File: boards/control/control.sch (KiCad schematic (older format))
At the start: 73 parts, among them U1 SN74ACT08PW, U10 MC74ACT139DG, U11 SN74ACT08PW, U12 SN74ACT08PW, U13 SN74ACT32PW, U14 74ACT00MTCX, U15 MC74ACT139DG, U16 SN74ACT32PW, U2 MC74ACT139DG, U3 MC74ACT86DG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

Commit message: Fix bug in CU schematics
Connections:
- wire segments 122 -> 125
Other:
- moved on the sheet: U16C, U9A
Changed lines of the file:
@@
 L 74xx:74HC00 U9
 U 1 1 5E83EE30
-P 6200 3600
-F 0 "U9" H 6200 3925 50  0000 C CNN
-F 1 "74ACT00MTCX" H 6200 3834 50  0000 C CNN
-F 2 "Package_SO:TSSOP-14_4.4x5mm_P0.65mm" H 6200 3600 50  0001 C CNN
-F 3 "http://www.ti.com/lit/gpn/sn74hc00" H 6200 3600 50  0001 C CNN
-	1    6200 3600
+P 6950 3600
+F 0 "U9" H 6950 3925 50  0000 C CNN
+F 1 "74ACT00MTCX" H 6950 3834 50  0000 C CNN
+F 2 "Package_SO:TSSOP-14_4.4x5mm_P0.65mm" H 6950 3600 50  0001 C CNN
+F 3 "http://www.ti.com/lit/gpn/sn74hc00" H 6950 3600 50  0001 C CNN
+	1    6950 3600
 	1    0    0    -1
 $EndComp
@@
 Text Label 5900 3700 2    50   ~ 0
 ~cycle
-Text Label 6500 3600 0    50   ~ 0
+Text Label 7250 3600 0    50   ~ 0
 ~oe_mem
 Text Label 5900 4050 2    50   ~ 0
@@
 L 74xx:74LS32 U16
 U 3 1 5EAB37A5
-P 8150 12500
-F 0 "U16" H 8150 12825 50  0000 C CNN
-F 1 "SN74ACT32PW" H 8150 12734 50  0000 C CNN
-F 2 "Package_SO:TSSOP-14_4.4x5mm_P0.65mm" H 8150 12500 50  0001 C CNN
-F 3 "http://www.ti.com/lit/gpn/sn74LS32" H 8150 12500 50  0001 C CNN
-	3    8150 12500
+P 6200 3600
+F 0 "U16" H 6200 3925 50  0000 C CNN
+F 1 "SN74ACT32PW" H 6200 3834 50  0000 C CNN
+F 2 "Package_SO:TSSOP-14_4.4x5mm_P0.65mm" H 6200 3600 50  0001 C CNN
+F 3 "http://www.ti.com/lit/gpn/sn74LS32" H 6200 3600 50  0001 C CNN
+	3    6200 3600
 	1    0    0    -1
 $EndComp
@@
 Wire Wire Line
 	2800 4150 2750 4150
+Wire Wire Line
+	6500 3600 6650 3600
+Wire Wire Line
+	6650 3600 6650 3500
+Wire Wire Line
+	6650 3700 6650 3600
 Wire Bus Line
 	3750 2050 3750 2650
 Wire Bus Line
 	3750 1150 3750 1950
+Connection ~ 6650 3600
 $EndSCHEMATC

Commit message: Change control unit schematics to support wait cycles (not checked)
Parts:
- added C11, C12: 0.1u, Capacitor_SMD:C_0805_2012Metric, symbol Device:C
- added D23: KP-2012EC, LED_SMD:LED_0805_2012Metric, symbol Device:LED
- added R23: 620, Resistor_SMD:R_0805_2012Metric, symbol Device:R
- added U17: SN74ACT74D, Package_SO:SOIC-14_3.9x8.7mm_P1.27mm, symbol 74xx:74HC74
- added U18: 74HC02, symbol 74xx:74HC02
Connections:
- net labels added: cycle_d, mem_rdy, we_cycle_d, ~cycle_flip_ena, ~mem_rdy
- wire segments 125 -> 136
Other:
- moved on the sheet: U14C, U3B, U3D

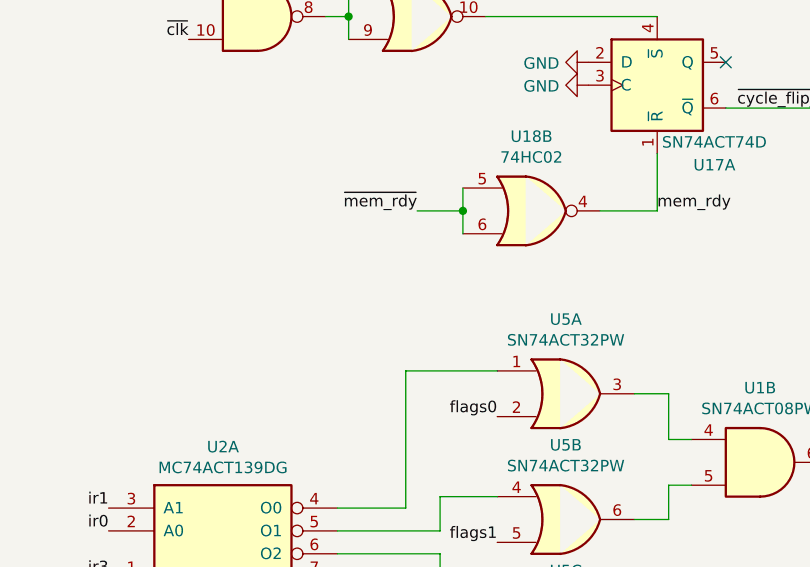
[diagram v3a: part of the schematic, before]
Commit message: Make n_rdy an open-drain pull-up
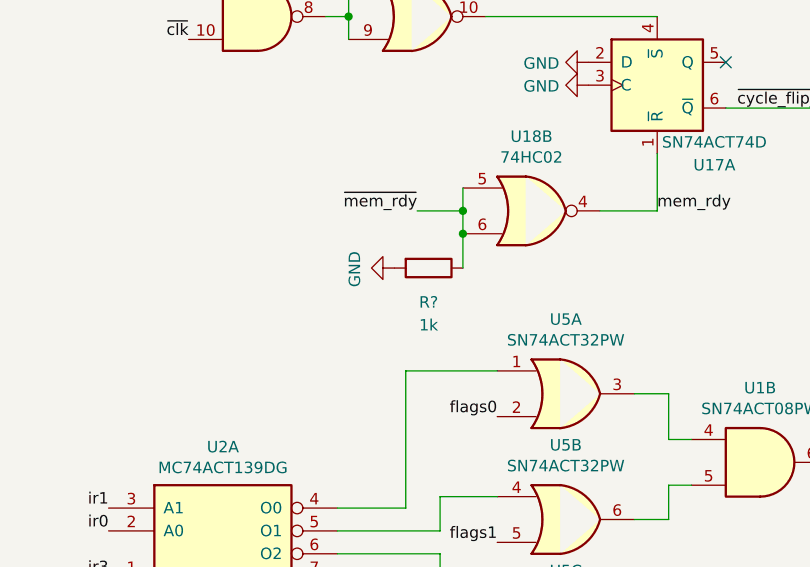
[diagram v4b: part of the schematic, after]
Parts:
- added R?: 1k, Resistor_SMD:R_0805_2012Metric, symbol Device:R
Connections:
- wire segments 136 -> 137
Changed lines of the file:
@@
 	1    0    0    -1
 $EndComp
+Text Label 5050 5850 3    50   ~ 0
+we_cycle_d
+Text Label 1300 8700 1    50   ~ 0
+cycle_d
+$Comp
+L Device:R R?
+U 1 1 60425BE5
+P 2400 10850
+F 0 "R?" V 2550 10850 50  0000 C CNN
+F 1 "1k" V 2650 10850 50  0000 C CNN
+F 2 "Resistor_SMD:R_0805_2012Metric" V 2330 10850 50  0001 C CNN
+F 3 "~" H 2400 10850 50  0001 C CNN
+	1    2400 10850
+	0    1    1    0
+$EndComp
+Wire Wire Line
+	2550 10850 2550 10700
 Wire Bus Line
 	3750 2050 3750 2650
 Wire Bus Line
 	3750 1150 3750 1950
-Text Label 5050 5850 3    50   ~ 0
-we_cycle_d
-Text Label 1300 8700 1    50   ~ 0
-cycle_d
+Connection ~ 2550 10700
+$Comp
+L power:GND #PWR?
+U 1 1 6042F712
+P 2250 10850
+F 0 "#PWR?" H 2250 10600 50  0001 C CNN
+F 1 "GND" H 2255 10677 50  0000 C CNN
+F 2 "" H 2250 10850 50  0001 C CNN
+F 3 "" H 2250 10850 50  0001 C CNN
+	1    2250 10850
+	0    1    1    0
+$EndComp
 $EndSCHEMATC

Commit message: Control: change 74ACT with 74LV-A
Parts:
- U1, U11, U12: value SN74ACT08PW -> 74LV08APWJ
- U10, U15, U2: value MC74ACT139DG -> SN74LV139APWR; footprint Package_SO:SOIC-16_3.9x9.9mm_P1.27mm -> Package_SO:TSSOP-16_4.4x5mm_P0.65mm
- U13, U16, U5, U8: value SN74ACT32PW -> 74LV32APWJ
- U14, U9: value 74ACT00MTCX -> SN74LV00APW
- U17, U4, U6: value SN74ACT74D -> SN74LV74APW; footprint Package_SO:SOIC-14_3.9x8.7mm_P1.27mm -> Package_SO:TSSOP-14_4.4x5mm_P0.65mm
- U18: value 74HC02 -> SN74LV02APWR; footprint (none) -> Package_SO:TSSOP-14_4.4x5mm_P0.65mm
- U3: value MC74ACT86DG -> SN74LV86APWR; footprint Package_SO:SOIC-14_3.9x8.7mm_P1.27mm -> Package_SO:TSSOP-14_4.4x5mm_P0.65mm
- U7: value SN74ACT04PW -> SN74LV04APWR

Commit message: Control: add more capacitors and damping resistors
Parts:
- added C13, C14, C15, C16, C17, C18, C19: 0.1u, Capacitor_SMD:C_0805_2012Metric, symbol Device:C
- added R24, R26: 50, Resistor_SMD:R_0805_2012Metric, symbol Device:R
- gave numbers to parts that had none: 1
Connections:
- wire segments 137 -> 138
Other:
- moved on the sheet: C1, C10, C11, C12, C2, C3, C5, C6, C7, C8, C9

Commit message: Control: PCB rev. 3
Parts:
- added D24: KP-2012CGCK, LED_SMD:LED_0805_2012Metric, symbol Device:LED
- added R27: 600, Resistor_SMD:R_0805_2012Metric, symbol Device:R
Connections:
- net labels added: cycle_flip_ena
- wire segments 138 -> 140
- no-connect marks 13 -> 11
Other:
- moved on the sheet: D21, R21
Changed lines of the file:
@@
 encoding utf-8
 Sheet 1 2
-Title "Control unit - ROM-based"
+Title "Control unit"
 Date "2020-11-29"
 Rev "3"
@@
 NoConn ~ 10650 13100
 $Comp
-L power:GND #PWR040
-U 1 1 60027546
-P 10050 13000
-F 0 "#PWR040" H 10050 12750 50  0001 C CNN
-F 1 "GND" V 10055 12872 50  0000 R CNN
-F 2 "" H 10050 13000 50  0001 C CNN
-F 3 "" H 10050 13000 50  0001 C CNN
-	1    10050 13000
-	0    1    1    0
-$EndComp
-$Comp
-L power:GND #PWR041
-U 1 1 60026D0E
-P 10050 13200
-F 0 "#PWR041" H 10050 12950 50  0001 C CNN
-F 1 "GND" V 10055 13072 50  0000 R CNN
-F 2 "" H 10050 13200 50  0001 C CNN
-F 3 "" H 10050 13200 50  0001 C CNN
-	1    10050 13200
-	0    1    1    0
-$EndComp
-$Comp
 L 74xx:74HC86 U3
 U 4 1 6001AAE8
@@
 Text Label 14700 3650 0    50   ~ 0
 ~we_flags
-NoConn ~ 5150 8600
 NoConn ~ 9550 13100
 NoConn ~ 8450 13150
-$Comp
-L power:GND #PWR0103
-U 1 1 5EB12FC5
-P 8950 13000
-F 0 "#PWR0103" H 8950 12750 50  0001 C CNN
-F 1 "GND" V 8955 12872 50  0000 R CNN
-F 2 "" H 8950 13000 50  0001 C CNN
-F 3 "" H 8950 13000 50  0001 C CNN
-	1    8950 13000
-	0    1    1    0
-$EndComp
-$Comp
-L power:GND #PWR0104
-U 1 1 5EB12FCB
-P 8950 13200
-F 0 "#PWR0104" H 8950 12950 50  0001 C CNN
-F 1 "GND" V 8955 13072 50  0000 R CNN
-F 2 "" H 8950 13200 50  0001 C CNN
-F 3 "" H 8950 13200 50  0001 C CNN
-	1    8950 13200
-	0    1    1    0
-$EndComp
-$Comp
-L power:GND #PWR0109
-U 1 1 5EB1F978
-P 7850 13050
-F 0 "#PWR0109" H 7850 12800 50  0001 C CNN
-F 1 "GND" V 7855 12922 50  0000 R CNN
-F 2 "" H 7850 13050 50  0001 C CNN
-F 3 "" H 7850 13050 50  0001 C CNN
-	1    7850 13050
-	0    1    1    0
-$EndComp
-$Comp
-L power:GND #PWR0110
-U 1 1 5EB1F97E
-P 7850 13250
-F 0 "#PWR0110" H 7850 13000 50  0001 C CNN
-F 1 "GND" V 7855 13122 50  0000 R CNN
-F 2 "" H 7850 13250 50  0001 C CNN
-F 3 "" H 7850 13250 50  0001 C CNN
-	1    7850 13250
-	0    1    1    0
-$EndComp
 Wire Wire Line
 	4550 8700 2700 8700
@@
 L Device:LED D21
 U 1 1 5EBF0DA9
-P 5750 8800
-F 0 "D21" H 5750 8650 50  0000 C CNN
-F 1 "KP-2012CGCK" H 5743 8925 50  0001 C CNN
-F 2 "LED_SMD:LED_0805_2012Metric" H 5750 8800 50  0001 C CNN
-F 3 "~" H 5750 8800 50  0001 C CNN
-	1    5750 8800
-	1    0    0    -1
+P 5800 8600
+F 0 "D21" H 5800 8450 50  0000 C CNN
+F 1 "KP-2012CGCK" H 5793 8725 50  0001 C CNN
+F 2 "LED_SMD:LED_0805_2012Metric" H 5800 8600 50  0001 C CNN
+F 3 "~" H 5800 8600 50  0001 C CNN
+	1    5800 8600
+	-1   0    0    1
 $EndComp
 $Comp
 L Device:R R21
 U 1 1 5EBF0DAF
-P 6050 8800
-F 0 "R21" V 6200 8800 50  0000 C CNN
-F 1 "600" V 6300 8800 50  0000 C CNN
-F 2 "Resistor_SMD:R_0805_2012Metric" V 5980 8800 50  0001 C CNN
-F 3 "~" H 6050 8800 50  0001 C CNN
-	1    6050 8800
+P 6100 8600
+F 0 "R21" V 6250 8600 50  0000 C CNN
+F 1 "600" V 6350 8600 50  0000 C CNN
+F 2 "Resistor_SMD:R_0805_2012Metric" V 6030 8600 50  0001 C CNN
+F 3 "~" H 6100 8600 50  0001 C CNN
+	1    6100 8600
 	0    1    1    0
 $EndComp
 $Comp
-L power:VCC #PWR078
-U 1 1 5EBF0DB5
-P 6200 8800
-F 0 "#PWR078" H 6200 8650 50  0001 C CNN
-F 1 "VCC" V 6217 8928 50  0000 L CNN
-F 2 "" H 6200 8800 50  0001 C CNN
-F 3 "" H 6200 8800 50  0001 C CNN
-	1    6200 8800
-	0    1    1    0
-$EndComp
-Wire Wire Line
-	5600 8800 5150 8800
-$Comp
 L Device:LED D22
 U 1 1 5EBFD213
@@
 $Comp
 L 74xx:74HC74 U17
-U 1 1 60DE8A07
-P 3400 10050
-F 0 "U17" H 3650 9700 50  0000 C CNN
-F 1 "SN74LV74APW" H 3650 9800 50  0000 C CNN
-F 2 "Package_SO:TSSOP-14_4.4x5mm_P0.65mm" H 3400 10050 50  0001 C CNN
-F 3 "https://www.ti.com/lit/ds/symlink/sn74lv74a.pdf" H 3400 10050 50  0001 C CNN
-	1    3400 10050
-	1    0    0    -1
-$EndComp
-$Comp
-L 74xx:74HC74 U17
 U 2 1 60DEA5EB
 P 11500 12400
@@
 	1    0    0    -1
 $EndComp
-NoConn ~ 3700 9950
 $Comp
 L power:GND #PWR088
@@
 	1    0    0    -1
 $EndComp
+$Comp
+L Device:LED D24
+U 1 1 5FDE5646
+P 3950 9650
+F 0 "D24" H 3950 9500 50  0000 C CNN
+F 1 "KP-2012CGCK" H 3943 9775 50  0001 C CNN
+F 2 "LED_SMD:LED_0805_2012Metric" H 3950 9650 50  0001 C CNN
+F 3 "~" H 3950 9650 50  0001 C CNN
+	1    3950 9650
+	-1   0    0    1
+$EndComp
+$Comp
+L Device:R R27
+U 1 1 5FDE564C
+P 4250 9650
+F 0 "R27" V 4400 9650 50  0000 C CNN
+F 1 "600" V 4500 9650 50  0000 C CNN
+F 2 "Resistor_SMD:R_0805_2012Metric" V 4180 9650 50  0001 C CNN
+F 3 "~" H 4250 9650 50  0001 C CNN
+	1    4250 9650
+	0    1    1    0
+$EndComp
+$Comp
+L power:GND #PWR0121
+U 1 1 5FDFA0FB
+P 4400 9650
+F 0 "#PWR0121" H 4400 9400 50  0001 C CNN
+F 1 "GND" V 4405 9522 50  0000 R CNN
+F 2 "" H 4400 9650 50  0001 C CNN
+F 3 "" H 4400 9650 50  0001 C CNN
+	1    4400 9650
+	0    -1   -1   0
+$EndComp
+$Comp
+L 74xx:74HC74 U17
+U 1 1 60DE8A07
+P 3400 10050
+F 0 "U17" H 3650 9700 50  0000 C CNN
+F 1 "SN74LV74APW" H 3650 9800 50  0000 C CNN
+F 2 "Package_SO:TSSOP-14_4.4x5mm_P0.65mm" H 3400 10050 50  0001 C CNN
+F 3 "https://www.ti.com/lit/ds/symlink/sn74lv74a.pdf" H 3400 10050 50  0001 C CNN
+	1    3400 10050
+	1    0    0    -1
+$EndComp
+Wire Wire Line
+	3700 9950 3800 9950
+Wire Wire Line
+	3800 9950 3800 9650
+Text Label 3800 9700 2    50   ~ 0
+cycle_flip_ena
+Wire Wire Line
+	5650 8600 5150 8600
+$Comp
+L power:GND #PWR0122
+U 1 1 5FF668E6
+P 6250 8600
+F 0 "#PWR0122" H 6250 8350 50  0001 C CNN
+F 1 "GND" V 6255 8472 50  0000 R CNN
+F 2 "" H 6250 8600 50  0001 C CNN
+F 3 "" H 6250 8600 50  0001 C CNN
+	1    6250 8600
+	0    -1   -1   0
+$EndComp
+$Comp
+L power:VCC #PWR0123
+U 1 1 602F63A6
+P 10050 13000
+F 0 "#PWR0123" H 10050 12850 50  0001 C CNN
+F 1 "VCC" H 10067 13173 50  0000 C CNN
+F 2 "" H 10050 13000 50  0001 C CNN
+F 3 "" H 10050 13000 50  0001 C CNN
+	1    10050 13000
+	0    -1   -1   0
+$EndComp
+$Comp
+L power:VCC #PWR0124
+U 1 1 602F6CEF
+P 10050 13200
+F 0 "#PWR0124" H 10050 13050 50  0001 C CNN
+F 1 "VCC" H 10067 13373 50  0000 C CNN
+F 2 "" H 10050 13200 50  0001 C CNN
+F 3 "" H 10050 13200 50  0001 C CNN
+	1    10050 13200
+	0    -1   -1   0
+$EndComp
+$Comp
+L power:VCC #PWR0103
+U 1 1 6031AD6D
+P 8950 13000
+F 0 "#PWR0103" H 8950 12850 50  0001 C CNN
+F 1 "VCC" H 8967 13173 50  0000 C CNN
+F 2 "" H 8950 13000 50  0001 C CNN
+F 3 "" H 8950 13000 50  0001 C CNN
+	1    8950 13000
+	0    -1   -1   0
+$EndComp
+$Comp
+L power:VCC #PWR0104
+U 1 1 6031AD73
+P 8950 13200
+F 0 "#PWR0104" H 8950 13050 50  0001 C CNN
+F 1 "VCC" H 8967 13373 50  0000 C CNN
+F 2 "" H 8950 13200 50  0001 C CNN
+F 3 "" H 8950 13200 50  0001 C CNN
+	1    8950 13200
+	0    -1   -1   0
+$EndComp
+$Comp
+L power:VCC #PWR?
+U 1 1 6037D172
+P 7850 13050
+F 0 "#PWR?" H 7850 12900 50  0001 C CNN
+F 1 "VCC" H 7867 13223 50  0000 C CNN
+F 2 "" H 7850 13050 50  0001 C CNN
+F 3 "" H 7850 13050 50  0001 C CNN
+	1    7850 13050
+	0    -1   -1   0
+$EndComp
+$Comp
+L power:VCC #PWR?
+U 1 1 6037D178
+P 7850 13250
+F 0 "#PWR?" H 7850 13100 50  0001 C CNN
+F 1 "VCC" H 7867 13423 50  0000 C CNN
+F 2 "" H 7850 13250 50  0001 C CNN
+F 3 "" H 7850 13250 50  0001 C CNN
+	1    7850 13250
+	0    -1   -1   0
+$EndComp
 Wire Bus Line
